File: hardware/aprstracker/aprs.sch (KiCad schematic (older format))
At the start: 122 parts, among them IC1 ATMEGA8-AI, J1 SMA, J2 SMA, P1 AVR ISP, P3 POWER 12V, Q1 MMBT5551, Q2 MMBT5551, Q3 BCX54, Q4 BFR93A, Q5 BFR93A, Q6 BFG135, Q7 MMBT5551, U1 LM7001, U2 EB-3531, U3 78L33, U4 78L05, X1 7.2Mhz, X2 14.7456Mhz

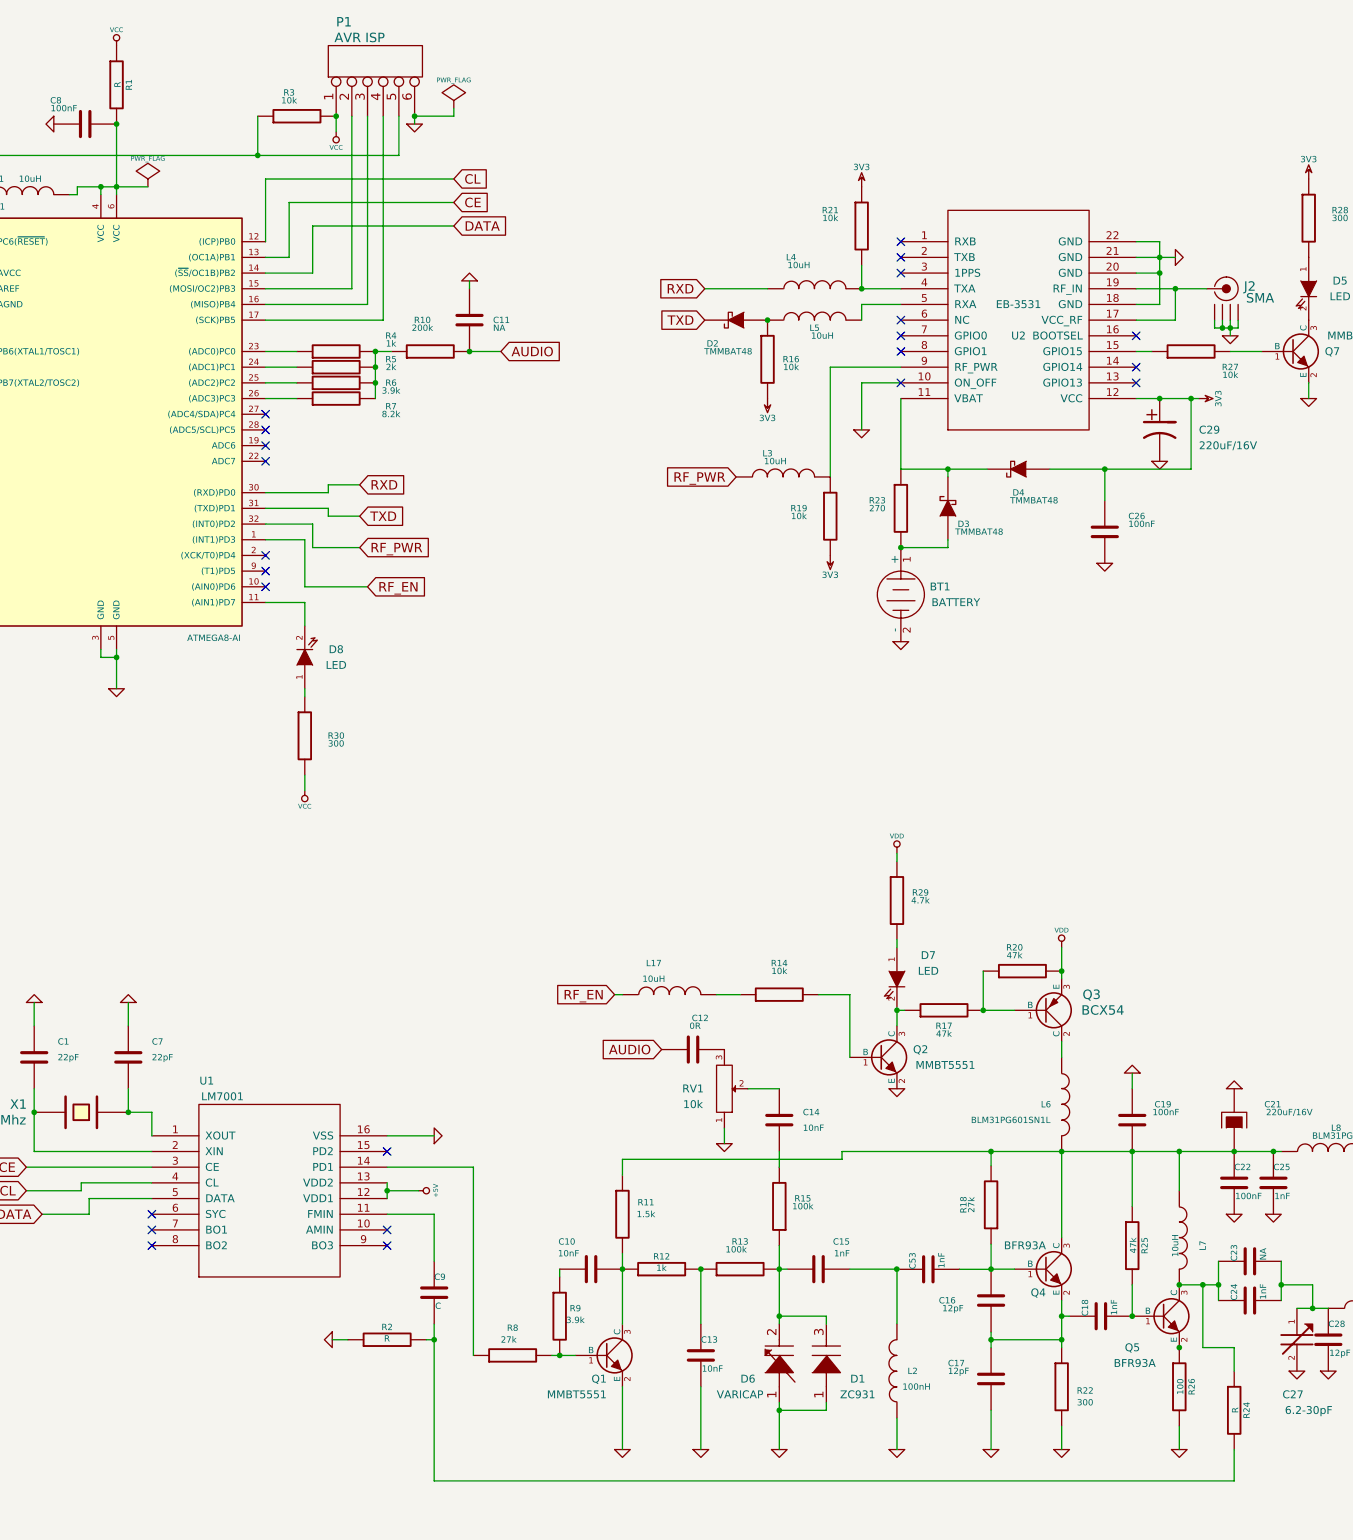
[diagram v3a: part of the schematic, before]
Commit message: [HW] Update values. Add capacitor to suppress negative feedback
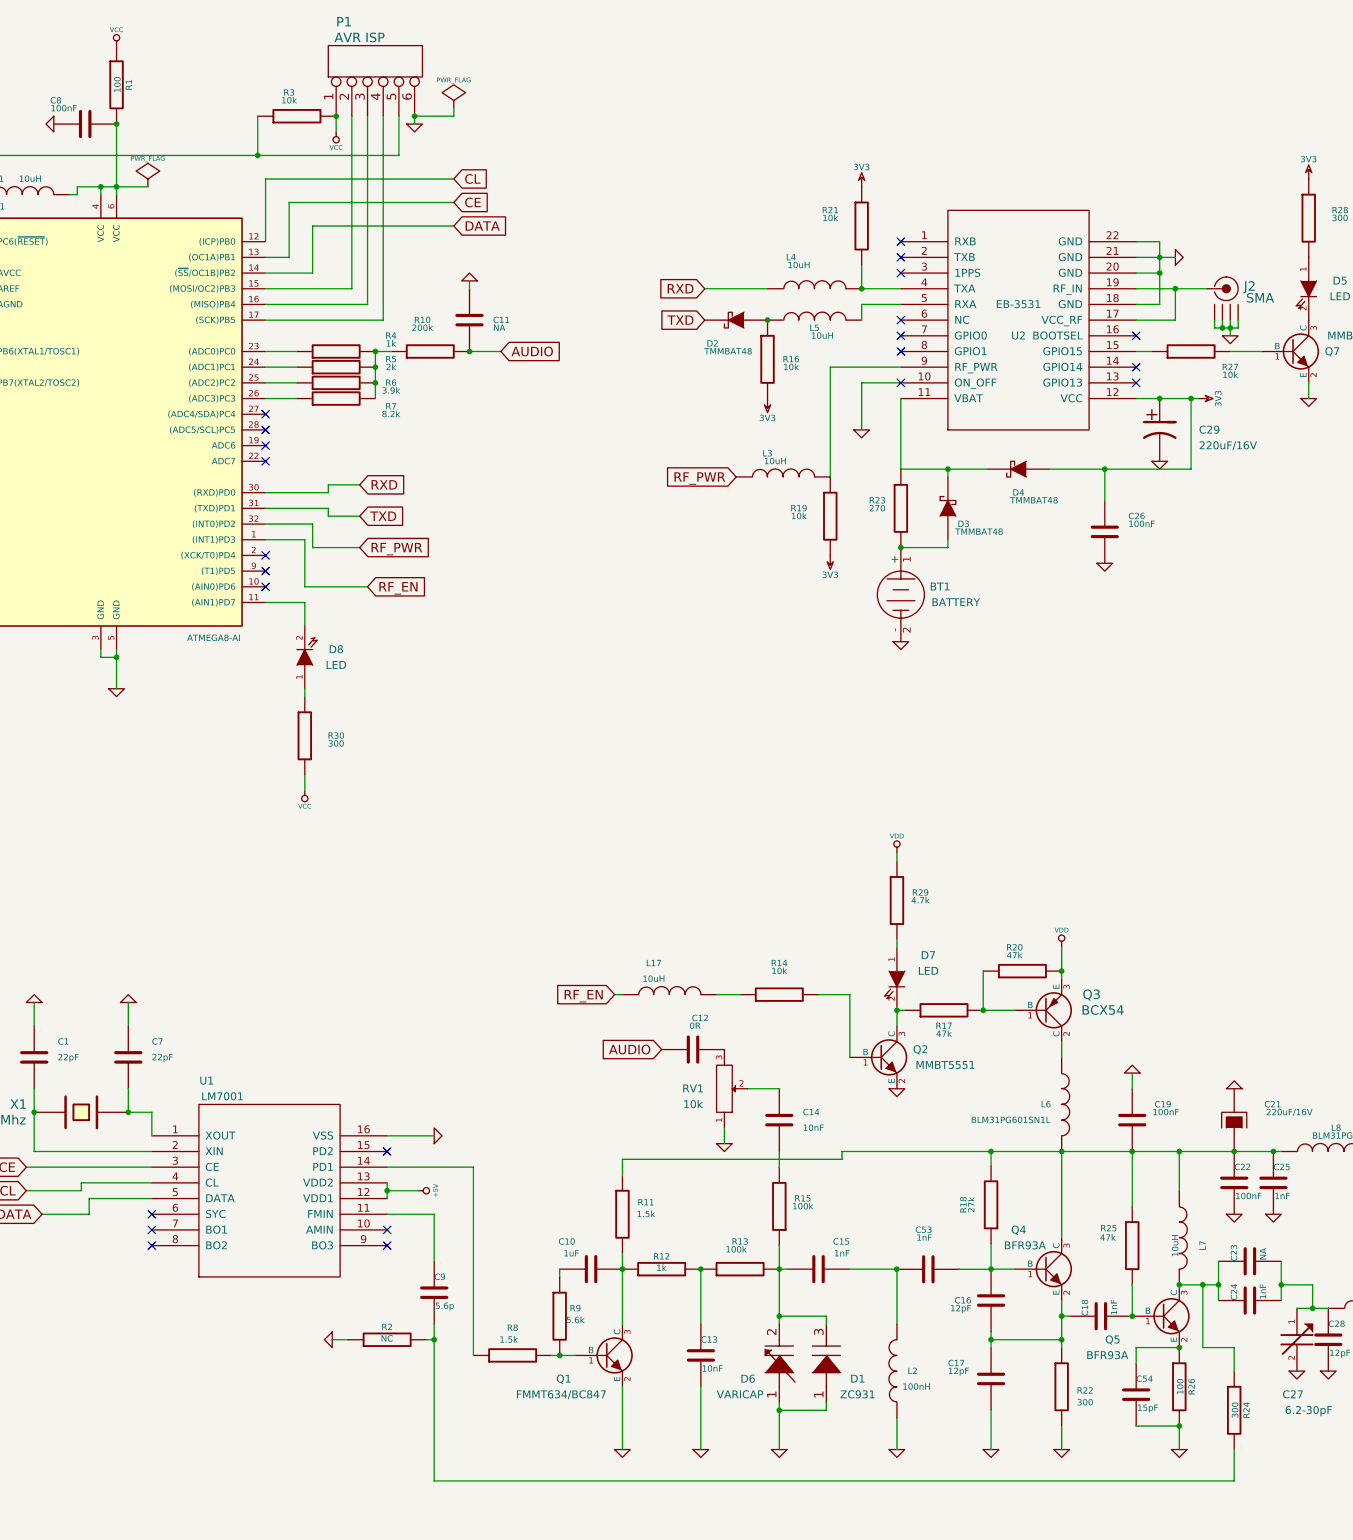
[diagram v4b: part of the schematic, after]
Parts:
- added C54: 15pF, ~, symbol C
- C10: value 10nF -> 1uF
- C9: value C -> 5.6p
- Q1: value MMBT5551 -> FMMT634/BC847
- R1: value R -> 100
- R2: value R -> NC
- R24: value R -> 300
- R8: value 27k -> 1.5k
- R9: value 3.9k -> 5.6k
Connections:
- net GND: now also C54.2
- net at Q5.2 (E), R26.1: now also C54.1
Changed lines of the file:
@@
-EESchema Schematic File Version 2  date Sun 15 Dec 2013 03:07:07 AM EET
+EESchema Schematic File Version 2  date Sun 15 Dec 2013 09:57:07 PM EET
 LIBS:power
 LIBS:device
@@
 U 1 1 519FD4BB
 P 8125 8900
-F 0 "C16" H 8350 8900 40  0000 L CNN
-F 1 "12pF" H 8300 8950 40  0000 L CNN
+F 0 "C16" H 8250 8900 40  0000 L CNN
+F 1 "12pF" H 8250 8950 40  0000 L CNN
 F 2 "SM0805" H 8163 8750 30  0001 C CNN
 F 3 "~" H 8125 8900 60  0000 C CNN
@@
 P 5375 9000
 F 0 "R9" H 5475 9050 40  0000 C CNN
-F 1 "3.9k" H 5475 8975 40  0000 C CNN
+F 1 "5.6k" H 5475 8975 40  0000 C CNN
 F 2 "SM0805" V 5305 9000 30  0001 C CNN
 F 3 "~" H 5375 9000 30  0000 C CNN
@@
 P 5575 8700
 F 0 "C10" V 5750 8800 40  0000 L CNN
-F 1 "10nF" V 5675 8775 40  0000 L CNN
+F 1 "1uF" V 5675 8775 40  0000 L CNN
 F 2 "SM0805" H 5613 8550 30  0001 C CNN
 F 3 "~" H 5575 8700 60  0000 C CNN
@@
 P 5075 9250
 F 0 "R8" V 5250 9250 40  0000 C CNN
-F 1 "27k" V 5175 9275 40  0000 C CNN
+F 1 "1.5k" V 5175 9275 40  0000 C CNN
 F 2 "SM0805" V 5005 9250 30  0001 C CNN
 F 3 "~" H 5075 9250 30  0000 C CNN
@@
 P 9675 9600
 F 0 "R24" V 9755 9600 40  0000 C CNN
-F 1 "R" V 9682 9601 40  0000 C CNN
+F 1 "300" V 9682 9601 40  0000 C CNN
 F 2 "SM0805" V 9605 9600 30  0001 C CNN
 F 3 "~" H 9675 9600 30  0000 C CNN
@@
 P 4575 8850
 F 0 "C9" H 4575 8950 40  0000 L CNN
-F 1 "C" H 4581 8765 40  0000 L CNN
+F 1 "5.6p" H 4581 8765 40  0000 L CNN
 F 2 "SM0805" H 4613 8700 30  0001 C CNN
 F 3 "~" H 4575 8850 60  0000 C CNN
@@
 P 4275 9150
 F 0 "R2" V 4355 9150 40  0000 C CNN
-F 1 "R" V 4282 9151 40  0000 C CNN
+F 1 "NC" V 4282 9151 40  0000 C CNN
 F 2 "SM0805" V 4205 9150 30  0001 C CNN
 F 3 "~" H 4275 9150 30  0000 C CNN
@@
 P 2550 1150
 F 0 "R1" V 2630 1150 40  0000 C CNN
-F 1 "R" V 2557 1151 40  0000 C CNN
+F 1 "100" V 2557 1151 40  0000 C CNN
 F 2 "SM0805" V 2480 1150 30  0001 C CNN
 F 3 "~" H 2550 1150 30  0000 C CNN
@@
 U 1 1 51A3B84E
 P 9025 8550
-F 0 "R25" V 9105 8550 40  0000 C CNN
-F 1 "47k" V 9032 8551 40  0000 C CNN
+F 0 "R25" H 8875 8660 40  0000 C CNN
+F 1 "47k" H 8870 8600 40  0000 C CNN
 F 2 "SM0805" V 8955 8550 30  0001 C CNN
 F 3 "~" H 9025 8550 30  0000 C CNN
@@
 U 1 1 51AD01CC
 P 9225 9000
-F 0 "Q5" H 9075 8800 50  0000 R CNN
-F 1 "BFR93A" H 9175 8700 50  0000 R CNN
+F 0 "Q5" H 8950 8850 50  0000 R CNN
+F 1 "BFR93A" H 9000 8750 50  0000 R CNN
 F 2 "SOT23" H 9225 9000 60  0001 C CNN
 F 3 "" H 9225 9000 60  0000 C CNN
@@
 U 1 1 51AD01F1
 P 8475 8700
-F 0 "Q4" H 8475 8550 50  0000 R CNN
+F 0 "Q4" H 8350 8950 50  0000 R CNN
 F 1 "BFR93A" H 8475 8850 50  0000 R CNN
 F 2 "SOT23" H 8475 8700 60  0001 C CNN
@@
 U 1 1 51AD1854
 P 5675 9250
-F 0 "Q1" H 5675 9100 50  0000 R CNN
-F 1 "MMBT5551" H 5675 9000 50  0000 R CNN
+F 0 "Q1" H 5450 9100 50  0000 R CNN
+F 1 "FMMT634/BC847" H 5675 9000 50  0000 R CNN
 F 2 "SOT23" H 5675 9250 60  0001 C CNN
 F 3 "" H 5675 9250 60  0000 C CNN
@@
 U 1 1 52A38A71
 P 7725 8701
-F 0 "C53" H 7725 8801 40  0000 L CNN
-F 1 "1nF" H 7731 8616 40  0000 L CNN
+F 0 "C53" V 7976 8676 40  0000 L CNN
+F 1 "1nF" V 7926 8676 40  0000 L CNN
 F 2 "SM0805" H 7763 8551 30  0001 C CNN
 F 3 "~" H 7725 8701 60  0000 C CNN
@@
 	8125 8040 8125 7950
 Connection ~ 8125 7950
+$Comp
+L C C54
+U 1 1 52AE0730
+P 9050 9500
+F 0 "C54" H 9050 9600 40  0000 L CNN
+F 1 "15pF" H 9056 9415 40  0000 L CNN
+F 2 "~" H 9088 9350 30  0000 C CNN
+F 3 "~" H 9050 9500 60  0000 C CNN
+	1    9050 9500
+	1    0    0    -1
+$EndComp
+Wire Wire Line
+	9050 9300 9050 9200
+Wire Wire Line
+	9050 9200 9325 9200
+Wire Wire Line
+	9050 9700 9325 9700
+Connection ~ 9325 9700
 $EndSCHEMATC

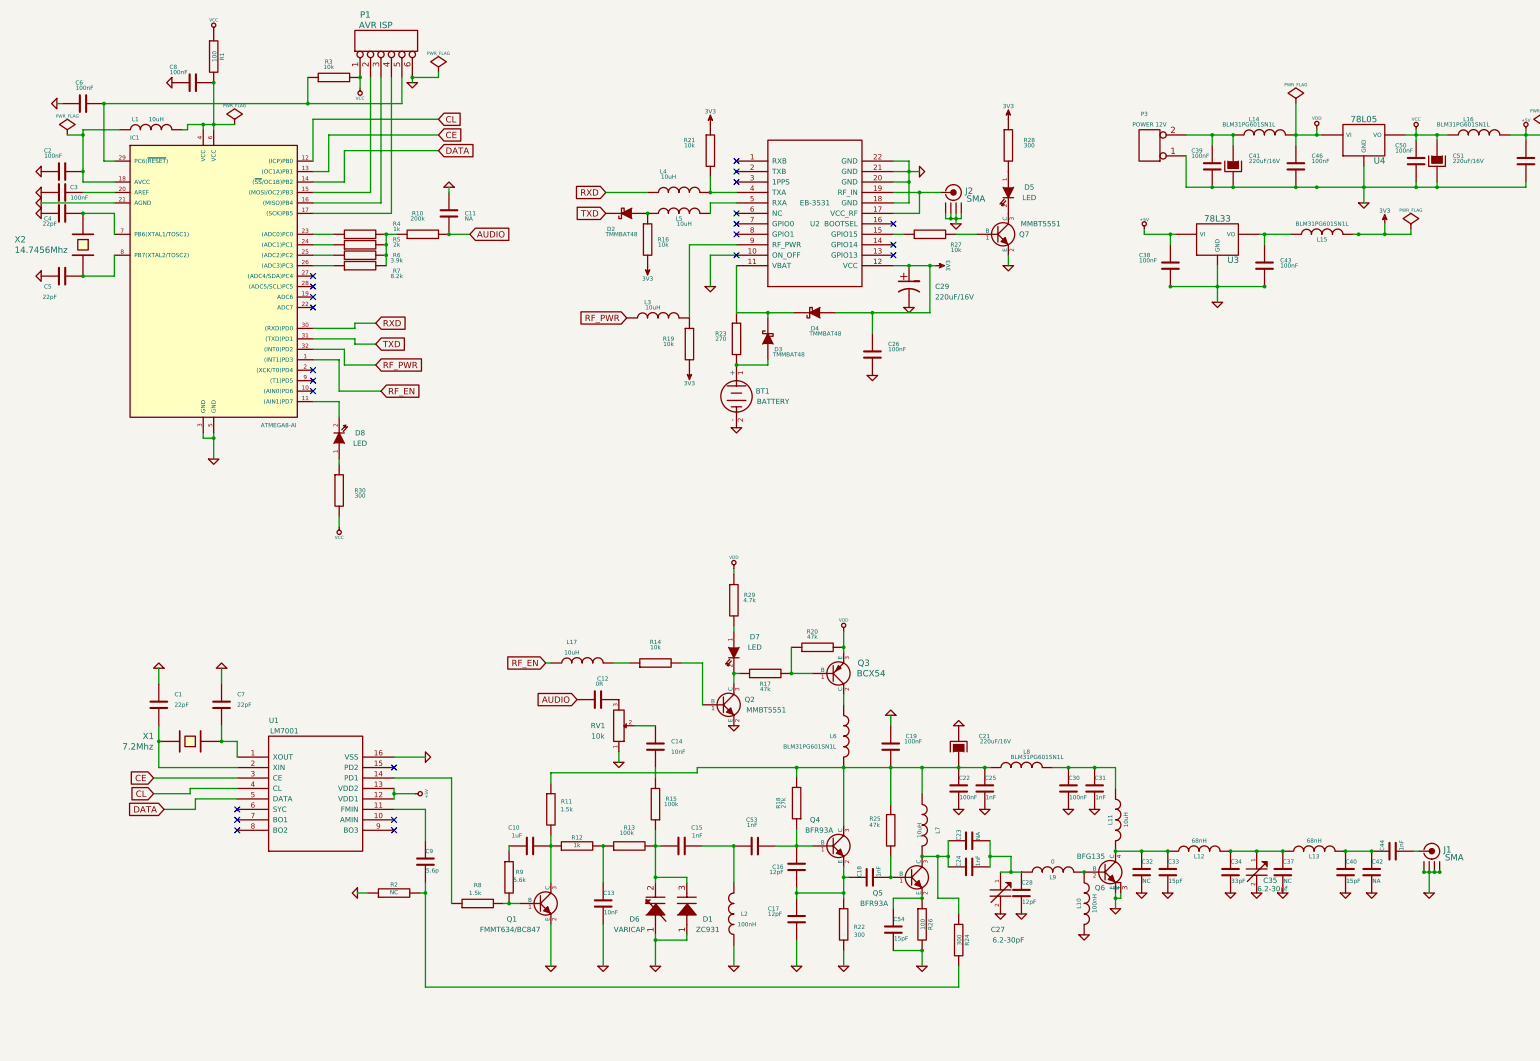
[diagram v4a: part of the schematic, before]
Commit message: Update sch elements values
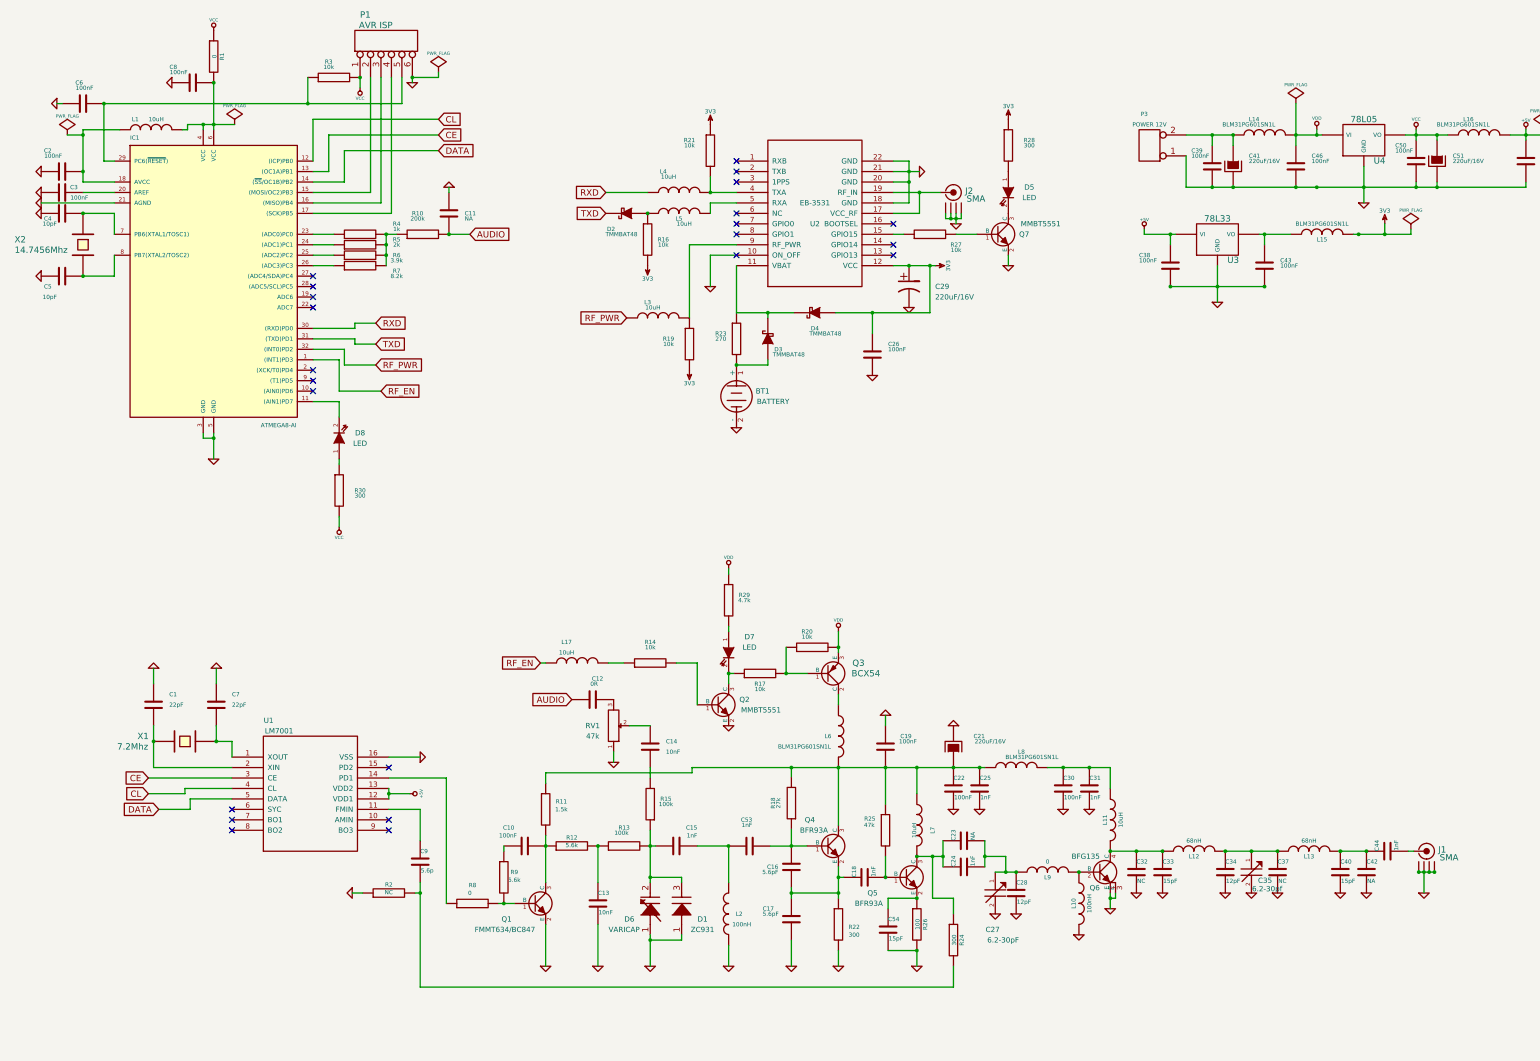
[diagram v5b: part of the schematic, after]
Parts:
- C10: value 1uF -> 100nF
- C16, C17: value 12pF -> 5.6pF
- C34: value 33pF -> 12pF
- C4, C5: value 22pF -> 10pF
- R1: value 100 -> 0
- R12: value 1k -> 5.6k
- R17, R20: value 47k -> 10k
- R8: value 1.5k -> 0
- RV1: value 10k -> 47k
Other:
- moved on the sheet: C1, C10, C12, C13, C14, C15, C16, C17, C18, C19, C21, C22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

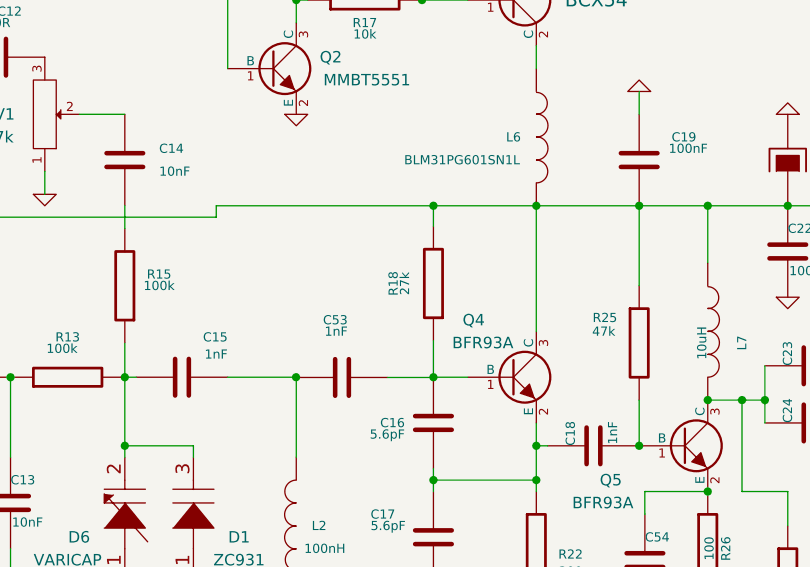
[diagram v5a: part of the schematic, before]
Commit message: [HW] Fix element values
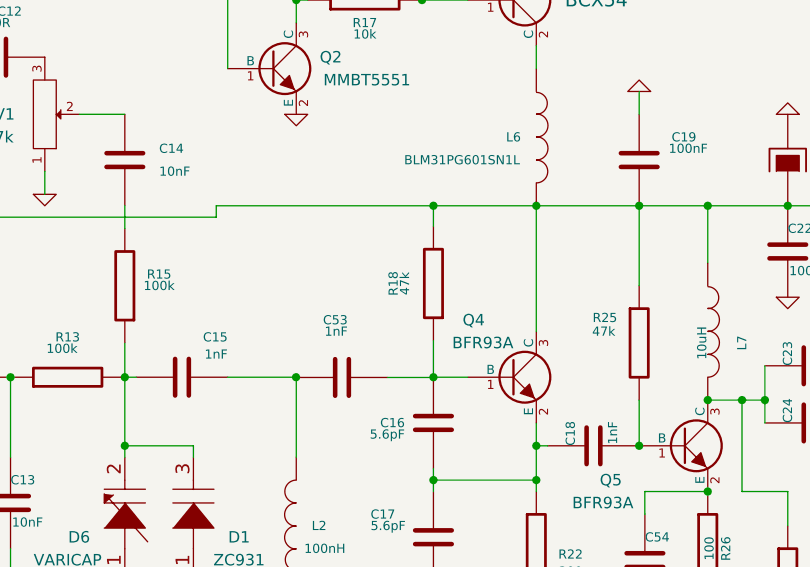
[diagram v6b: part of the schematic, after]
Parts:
- R18: value 27k -> 47k
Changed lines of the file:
@@
-EESchema Schematic File Version 2  date Sat 04 Jan 2014 11:49:45 PM EET
+EESchema Schematic File Version 2  date Sun 05 Jan 2014 01:50:47 AM EET
 LIBS:power
 LIBS:device
@@
 P 8075 8290
 F 0 "R18" V 8250 8290 40  0000 C CNN
-F 1 "27k" V 8200 8290 40  0000 C CNN
+F 1 "47k" V 8200 8290 40  0000 C CNN
 F 2 "SM0805" V 8005 8290 30  0001 C CNN
 F 3 "~" H 8075 8290 30  0000 C CNN
